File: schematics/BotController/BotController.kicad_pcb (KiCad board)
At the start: 2 copper layers, 29 parts, among them IC1 ATMEGA644A-P, P1 UM2102 - UART2USB, P10 Stepper Upperarm, P11 Stepper Shoulder, P2 Herkulex Servo, P3 Encoder Socket 0, P4 Encoder Socket, P5 Stepper 1 WristTurn, P6 POWER uC, P7 POWER_SERVO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

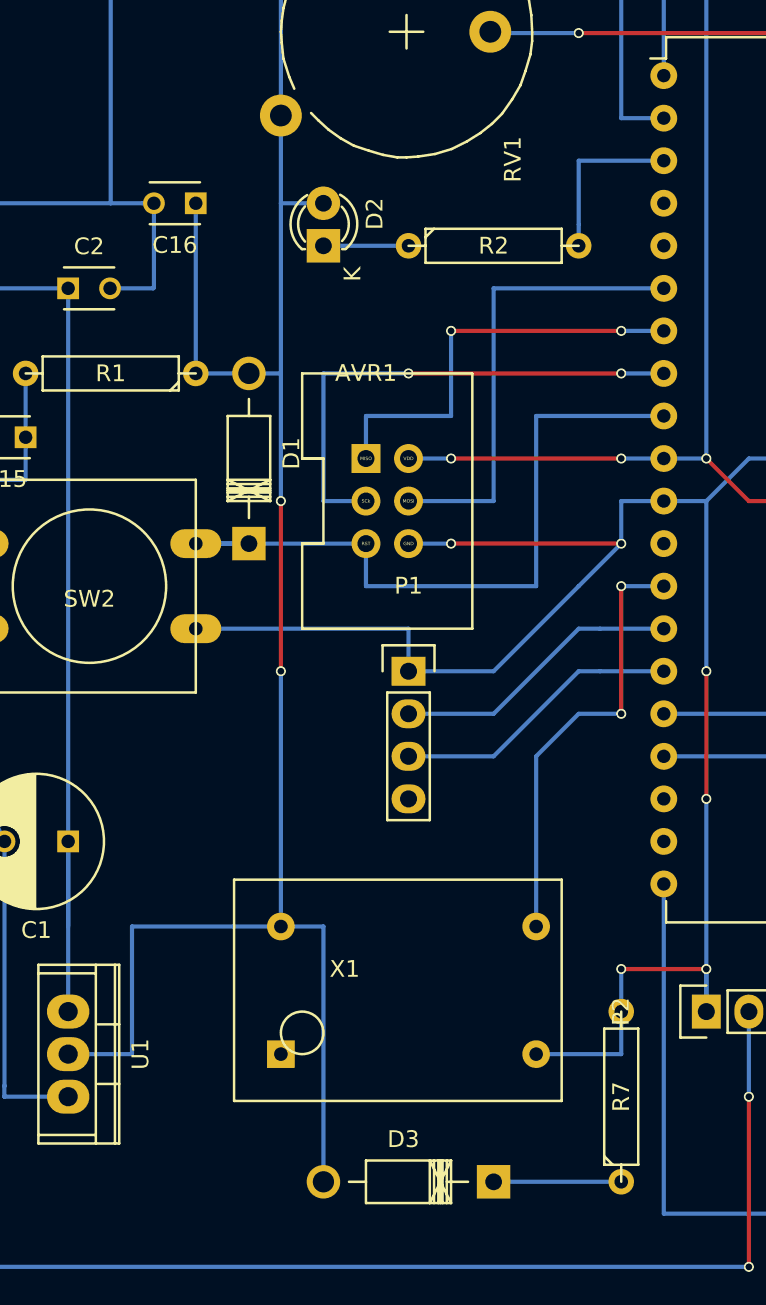
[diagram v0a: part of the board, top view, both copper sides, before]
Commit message: PCB bekommt die letzten 4 PINs als enhancement Stecker Handgelenk vom Rest des entfernbaren Motordecksl bereinigt
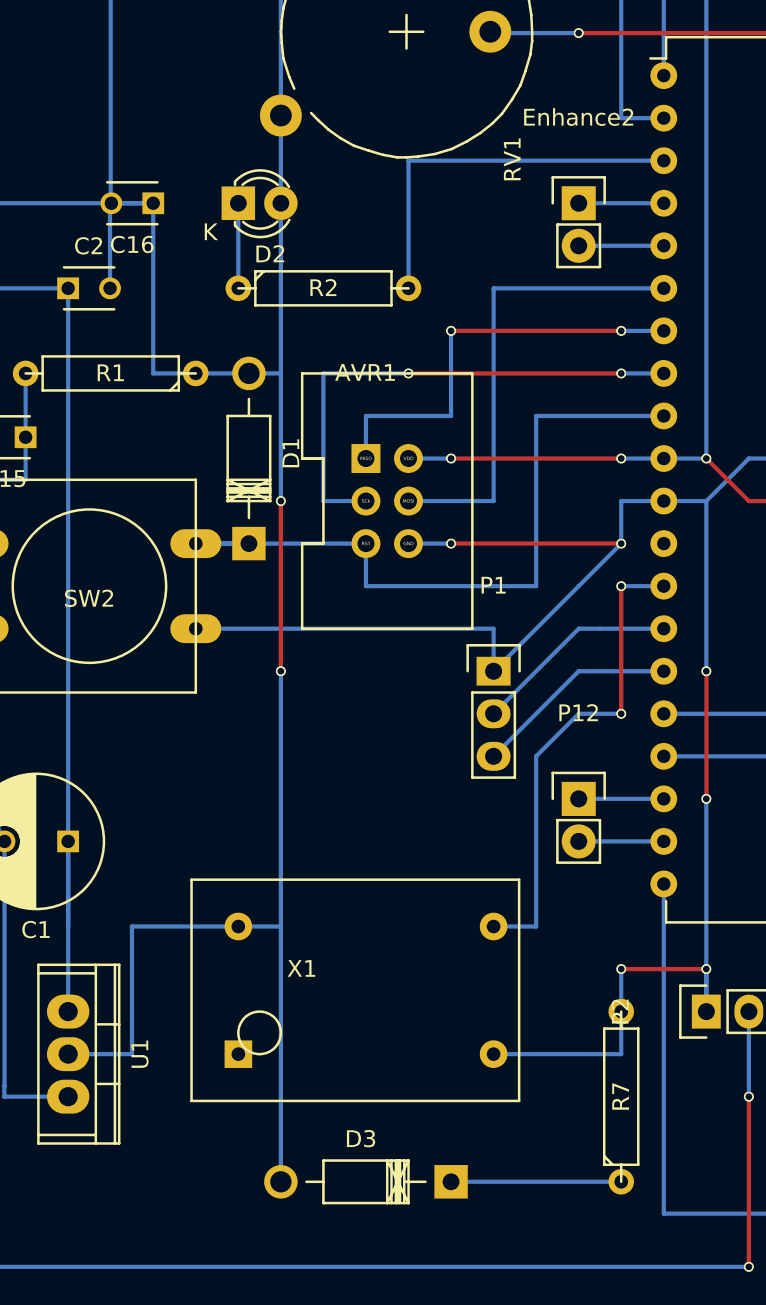
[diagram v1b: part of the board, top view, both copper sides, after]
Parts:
- added Enhance2: CONN_01X02, Pin_Headers:Pin_Header_Straight_1x02, F.Cu at (194.3, 96.5)
- added P12: Enhance1, Pin_Headers:Pin_Header_Straight_1x02, F.Cu at (194.3, 132.1)
- P1: footprint Pin_Headers:Pin_Header_Straight_1x04 -> Pin_Headers:Pin_Header_Straight_1x03
- moved R2 10.5 mm to (179.1, 101.6)
- moved D2 5.68 mm to (174.0, 96.5), turned to 0 degrees
- moved P1 5.08 mm to (189.2, 124.5)
- moved C16 2.54 mm to (168.9, 96.5)
- moved D3 2.54 mm to (186.7, 154.9)
- moved X1 2.54 mm to (177.8, 143.5)
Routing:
- net Net-(IC1-Pad3): track 10.2 -> 22.9 mm
- net Net-(IC1-Pad19): track 0.00 -> 5.08 mm
- net Net-(IC1-Pad18): track 0.00 -> 5.08 mm
- net Net-(Enhance2-Pad2): track 0.00 -> 5.08 mm
- net Net-(Enhance2-Pad1): track 0.00 -> 5.08 mm
- net /TXD0: track 17.3 -> 12.3 mm
- net /RXD0: track 17.3 -> 12.3 mm
- net /TAL: track 26.5 -> 29.0 mm
- net Net-(D3-Pad1): track 7.62 -> 10.2 mm
- net /+5V: track 274.7 -> 272.2 mm
- net GNDPWR: track 395.9 -> 397.0 mm

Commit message: Ellenbogen gedruckt und Schaltung mit PowerSupply gemacht
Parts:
- removed Enhance2: CONN_01X02, Pin_Headers:Pin_Header_Straight_1x02
- added C11: 100uF, Capacitors_ThroughHole:C_Radial_D7.5_L11.2_P2.5, F.Cu at (38.1, 99.1)
- added C12: 100nF, Capacitors_ThroughHole:C_Disc_D3_P2.5, F.Cu at (38.1, 106.7)
- added C13: 1000uF, Capacitors_ThroughHole:C_Radial_D7.5_L11.2_P2.5, F.Cu at (30.5, 116.8)
- added C14: 100nF, Capacitors_ThroughHole:C_Disc_D3_P2.5, F.Cu at (43.2, 119.4)
- added C7: 100uF, Capacitors_ThroughHole:C_Radial_D5_L6_P2.5, F.Cu at (188.0, 92.7)
- added D10: DIODE, Diodes_ThroughHole:Diode_DO-41_SOD81_Horizontal_RM10, F.Cu at (68.6, 119.4)
- added D5: 1N5822, Diodes_ThroughHole:Diode_DO-41_SOD81_Horizontal_RM10, F.Cu at (30.5, 109.2)
- added D9: DIODE, Diodes_ThroughHole:Diode_DO-41_SOD81_Horizontal_RM10, F.Cu at (50.8, 119.4)
- added F1: FUSE, Pin_Headers:Pin_Header_Straight_1x02, F.Cu at (22.9, 96.5)
- added P13: PowerEnableIn, Connectors_Molex:Molex_KK_6410-02, F.Cu at (207.0, 59.7)
- added P17: PowerEnableOut, Connectors_Molex:Molex_KK_6410-02, F.Cu at (61.0, 124.5)
- added P28: Power Stepper, Connect:bornier2, F.Cu at (86.4, 99.1)
- added Q1: Q_NPN_BCE, TO_SOT_Packages_THT:TO-92_Inline_Wide, F.Cu at (48.3, 124.5)
- added Q2: Q_NPN_BCE, TO_SOT_Packages_THT:TO-92_Inline_Wide, F.Cu at (66.0, 124.5)
- added R10: 1K, Discret:R4, F.Cu at (66.0, 129.5)
- added R5: 120, Discret:R4, F.Cu at (81.3, 109.2)
- added R6: 120, Discret:R4, F.Cu at (63.5, 109.2)
- added R8: 1K, Discret:R4, F.Cu at (53.3, 129.5)
- added REL1: Relay_1xON, BotController:RELAIS_HF115F, F.Cu at (55.9, 111.8)
- added REL2: Relay_1xON, BotController:RELAIS_HF115F, F.Cu at (73.7, 111.8)
- added U3: LM7809ACT, Power_Integrations:TO-220, F.Cu at (40.6, 114.3)
- P12: value Enhance1 -> POWER_IN; footprint Pin_Headers:Pin_Header_Straight_1x02 -> Connect:bornier4
- P6: value POWER uC -> Power In uC Servo; footprint Connect:bornier2 -> Connectors_Molex:Molex_KK_6410-03
- P7: value POWER_SERVO -> Power Out uC Servo; footprint Connect:bornier2 -> Connectors_Molex:Molex_KK_6410-03
- moved P12 172.6 mm to (22.9, 111.8), turned to 270 degrees
- moved P7 64.8 mm to (86.4, 114.3), turned to 270 degrees
- moved IC1 39.4 mm to (213.4, 52.1)
- moved P8 39.4 mm to (246.4, 57.1)
- moved R1 39.4 mm to (180.3, 69.8)
- moved R3 39.4 mm to (243.8, 115.6)
- moved R4 39.4 mm to (236.2, 101.6)
- moved R7 39.4 mm to (210.8, 113.0)
- moved AVR1 39.4 mm to (195.6, 74.9)
- moved C1 39.4 mm to (177.8, 97.8)
- moved D1 39.4 mm to (188.6, 80.0)
- moved D2 39.4 mm to (188.0, 59.7)
- moved D3 39.4 mm to (200.7, 118.1)
- moved P1 39.4 mm to (203.2, 87.6)
- moved P10 39.4 mm to (246.4, 77.5)
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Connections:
- C1 pad 1: Net-(C1-Pad1) -> /VDDuC
- C2 pad 1: Net-(C1-Pad1) -> /VDDuC
- IC1 pad 12: Net-(IC1-Pad12) -> (no net)
- IC1 pad 18: Net-(IC1-Pad18) -> (no net)
- IC1 pad 19: Net-(IC1-Pad19) -> (no net)
- P12 pad 1: Net-(IC1-Pad18) -> /24V
- P12 pad 2: Net-(IC1-Pad19) -> /12V
- P2 pad 2: Net-(P2-Pad2) -> /VDDServo
- P6 pad 1: Net-(C1-Pad1) -> GNDPWR
- P6 pad 2: GNDPWR -> /VDDuC
- P7 pad 1: Net-(P2-Pad2) -> /VDD_Servo
- P7 pad 2: GNDPWR -> /VDD_uC
- U1 pad VI: Net-(C1-Pad1) -> /VDDuC
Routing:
- net /VDDServo: track 0.00 -> 132.5 mm, vias 0 -> 2
- net Net-(P2-Pad2): track 114.3 -> 0.00 mm, vias 4 -> 0
- net Net-(C1-Pad1): track 61.0 -> 0.00 mm
- net /VDDuC: track 0.00 -> 61.0 mm
- net GNDPWR: track 397.0 -> 338.7 mm
- net (no net): track 0.00 -> 10.2 mm
- net /RST: track 56.5 -> 65.4 mm
- net /+5V: track 272.2 -> 264.6 mm
- net Net-(IC1-Pad19): track 5.08 -> 0.00 mm
- net Net-(IC1-Pad18): track 5.08 -> 0.00 mm
- net Net-(IC1-Pad4): track 5.08 -> 6.35 mm

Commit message: HostCommunication scheint zu gehen
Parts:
- removed D3, D9: DIODE, Diodes_ThroughHole:Diode_DO-41_SOD81_Horizontal_RM10
- removed R7: 4,7K, Discret:R4
- added C3: 100uF, Capacitors_ThroughHole:C_Radial_D5_L6_P2.5, F.Cu at (88.9, 96.5)
- added C4: 10uF, Capacitors_ThroughHole:C_Radial_D5_L6_P2.5, F.Cu at (71.1, 119.4)
- added C5: 10uF, Capacitors_ThroughHole:C_Radial_D5_L6_P2.5, F.Cu at (64.8, 109.2)
- added D4: D, Diodes_ThroughHole:Diode_DO-35_SOD27_Horizontal_RM10, F.Cu at (185.4, 64.8)
- added P14: ENHANCE, Connectors_Molex:Molex_KK_6410-02, F.Cu at (208.3, 95.2)
- added U2: LM7809ACT, Power_Integrations:TO-220, F.Cu at (86.4, 88.9)
- D1, D10: value DIODE -> Diode; footprint Diodes_ThroughHole:Diode_DO-41_SOD81_Horizontal_RM10 -> Diodes_ThroughHole:Diode_DO-35_SOD27_Horizontal_RM10
- D5: footprint Diodes_ThroughHole:Diode_DO-41_SOD81_Horizontal_RM10 -> Diodes_ThroughHole:Diode_DO-35_SOD27_Horizontal_RM10
- F1: footprint Pin_Headers:Pin_Header_Straight_1x02 -> BotController:FUSE_HOLDER
- P1: footprint Pin_Headers:Pin_Header_Straight_1x03 -> Connectors_Molex:Molex_KK_6410-03
- P10, P11, P2, P3, P4, P5, P8, P9: footprint Pin_Headers:Pin_Header_Straight_1x04 -> Connectors_Molex:Molex_KK_6410-04
- X1: value CRYSTAL_OSSCI -> QUARZ_OSSCILATOR
- moved D1 130.9 mm to (61.0, 109.2), turned to 180 degrees
- moved F1 22.7 mm to (43.2, 86.4), turned to 90 degrees
- moved P28 22.7 mm to (96.5, 119.4), turned to 90 degrees
- moved Q2 20.5 mm to (86.4, 121.9), turned to 90 degrees
- moved C11 19.8 mm to (50.8, 114.3), turned to 90 degrees
- moved P7 18.3 mm to (96.5, 99.1), turned to 90 degrees
- moved P6 18.2 mm to (172.7, 55.9), turned to 180 degrees
- moved D5 16.1 mm to (45.7, 114.3)
- moved D10 12.7 mm to (78.7, 111.8), turned to 180 degrees
- moved C12 11.7 mm to (40.6, 118.1), turned to 180 degrees
- moved C14 10.5 mm to (33.0, 116.8), turned to 270 degrees
- moved R3 10.2 mm to (243.8, 105.4)
- moved R5 10.2 mm to (81.3, 99.1)
- moved P4 8.03 mm to (254.0, 100.3), turned to 180 degrees
- moved P9 8.03 mm to (254.0, 67.3), turned to 180 degrees
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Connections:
- net Net-(IC1-Pad4) renamed /PowerSupplyServo
- net Net-(IC1-Pad5) renamed /PowerSupplyStepper
- C13 pad 1: /VDD_uC -> Net-(C13-Pad1)
- C14 pad 1: /VDD_uC -> Net-(C13-Pad1)
- D1 pad 1: /RST -> Net-(C5-Pad2)
- D1 pad 2: /+5V -> Net-(D1-Pad2)
- D10 pad 1: Net-(D10-Pad1) -> Net-(C4-Pad2)
- D2 pad 1: Net-(D2-Pad1) -> /+5V
- D2 pad 2: /+5V -> Net-(D2-Pad2)
- D5 pad 1: /12V -> Net-(C11-Pad1)
- D5 pad 2: Net-(C11-Pad1) -> /12V
- IC1 pad 18: (no net) -> Net-(IC1-Pad18)
- IC1 pad 19: (no net) -> Net-(IC1-Pad19)
- P10 pad 1: /EN4 -> GNDPWR
- P10 pad 2: /DIR4 -> /CLK4
- P10 pad 3: /CLK4 -> /DIR4
- P10 pad 4: GNDPWR -> /EN4
- P11 pad 1: /En5 -> GNDPWR
- P11 pad 2: /DIR5 -> /CLK5
- P11 pad 3: /CLK5 -> /DIR5
- P11 pad 4: GNDPWR -> /En5
- P17 pad 1: Net-(P17-Pad1) -> /PowerOnStepper
- P17 pad 2: Net-(P17-Pad2) -> /PowerOnServo
- P3 pad 1: /ConflictEncoderVDD -> /ConflictEncoderGND
- P3 pad 2: /SCl -> /SDA
- P3 pad 3: /SDA -> /SCl
- P3 pad 4: /ConflictEncoderGND -> /ConflictEncoderVDD
- P4 pad 1: /+5V -> GNDPWR
- P4 pad 2: /SCl -> /SDA
- P4 pad 3: /SDA -> /SCl
- P4 pad 4: GNDPWR -> /+5V
- P5 pad 1: /EN1 -> GNDPWR
- P5 pad 2: /DIR1 -> /CLK1
- P5 pad 3: /CLK1 -> /DIR1
- P5 pad 4: GNDPWR -> /EN1
- P7 pad 1: /VDD_Servo -> GNDPWR
- P7 pad 3: GNDPWR -> /VDD_Servo
- P8 pad 1: /EN2 -> GNDPWR
- P8 pad 2: /DIR2 -> /CLK2
- P8 pad 3: /CLK2 -> /DIR2
- P8 pad 4: GNDPWR -> /EN2
- P9 pad 1: /EN3 -> GNDPWR
- P9 pad 2: /DIR3 -> /CLK3
- P9 pad 3: /CLK3 -> /DIR3
- P9 pad 4: GNDPWR -> /EN3
- Q1 pad 2: Net-(D9-Pad1) -> Net-(D1-Pad2)
- Q2 pad 2: Net-(D10-Pad1) -> Net-(D10-Pad2)
- R10 pad 2: Net-(P17-Pad1) -> /PowerOnServo
- R2 pad 1: Net-(D2-Pad1) -> Net-(D2-Pad2)
- R5 pad 1: Net-(D10-Pad2) -> Net-(C4-Pad2)
- R6 pad 1: Net-(D9-Pad2) -> Net-(C5-Pad2)
- R8 pad 2: Net-(P17-Pad2) -> /PowerOnStepper
- REL1 pad 1: Net-(D9-Pad1) -> Net-(D1-Pad2)
- REL1 pad 2: Net-(D9-Pad2) -> Net-(C5-Pad2)
- REL1 pad 3: /VDD_uC -> Net-(C13-Pad1)
- REL2 pad 1: Net-(D10-Pad1) -> Net-(D10-Pad2)
- REL2 pad 2: Net-(D10-Pad2) -> Net-(C4-Pad2)
- U3 pad 3: /VDD_uC -> Net-(C13-Pad1)
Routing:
- net Net-(C11-Pad1): track 0.00 -> 109.8 mm
- net Net-(C13-Pad1): track 0.00 -> 63.9 mm
- net GNDPWR: track 338.7 -> 400.3 mm, vias 8 -> 7
- net Net-(P28-Pad1): track 0.00 -> 61.0 mm, vias 0 -> 2
- net /VDD_Servo: track 0.00 -> 48.3 mm
- net /24V: track 0.00 -> 38.1 mm
- net Net-(D10-Pad2): track 0.00 -> 36.8 mm
- net Net-(D1-Pad2): track 0.00 -> 35.6 mm
- net Net-(F1-Pad2): track 0.00 -> 25.4 mm
- net Net-(C4-Pad2): track 0.00 -> 24.7 mm
- net /12V: track 0.00 -> 23.9 mm
- net Net-(C5-Pad2): track 0.00 -> 16.6 mm
- net /+5V: track 264.6 -> 249.3 mm
- net Net-(Q2-Pad1): track 0.00 -> 12.7 mm
- net /VDDuC: track 61.0 -> 72.4 mm
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
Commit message: stepper geht jetzt wieder
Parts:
- P14: value ENHANCE -> Logger
- moved P6 5.68 mm to (175.3, 50.8), turned to 270 degrees
- moved C15 2.54 mm to (175.3, 76.2)
- moved C2 2.54 mm to (172.7, 69.8)
- moved C13 1.27 mm to (26.7, 121.9)
- moved C14 1.27 mm to (31.8, 116.8)
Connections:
- net Net-(IC1-Pad18) renamed /LoggerTX
- IC1 pad 19: Net-(IC1-Pad19) -> (no net)
- P14 pad 2: Net-(IC1-Pad19) -> GNDPWR
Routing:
- net GNDPWR: track 400.3 -> 443.6 mm
- net /ConflictEncoderGND: track 144.8 -> 134.6 mm
- net /RST: track 70.5 -> 61.6 mm
- net Net-(IC1-Pad19): track 5.08 -> 0.00 mm
- net /DIR5: track 83.8 -> 78.7 mm
- net /CLK5: track 106.7 -> 101.6 mm
- net /VDDuC: track 72.4 -> 74.9 mm
- net /VDDServo: track 127.5 -> 125.7 mm, vias 2 -> 0
- net Net-(C13-Pad1): track 63.9 -> 62.6 mm

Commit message: no message
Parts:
- C3: value 100uF -> 220uF
- R3: footprint Discret:R4 -> BotController:R4(8)
- R4: footprint Discret:R5 -> BotController:R4(7)
- moved C2 27.4 mm to (182.9, 95.2), turned to 90 degrees
- moved R3 21.8 mm to (231.1, 87.6), turned to 270 degrees
- moved C15 14.2 mm to (188.0, 82.5), turned to 270 degrees
- moved R4 14.2 mm to (233.7, 87.6), turned to 270 degrees
- moved P2 2.54 mm to (215.9, 113.0)
- moved C16 2.54 mm to (190.5, 97.8)
- moved C7 2.54 mm to (190.5, 92.7)
- moved P10 2.54 mm to (251.5, 77.5)
- moved P11 2.54 mm to (251.5, 87.6)
- moved P3 2.54 mm to (251.5, 110.5)
- moved P4 2.54 mm to (251.5, 100.3)
- moved P5 2.54 mm to (251.5, 47.0)
- moved P8 2.54 mm to (251.5, 57.1)
- moved P9 2.54 mm to (251.5, 67.3)
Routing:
- net /DIR5: track 78.7 -> 27.5 mm, vias 0 -> 2
- net /En5: track 53.3 -> 17.3 mm
- net /SDA: track 76.2 -> 40.6 mm
- net /+5V: track 249.3 -> 228.6 mm, vias 11 -> 9
- net /CLK3: track 38.1 -> 26.6 mm
- net /TAL: track 30.5 -> 40.6 mm
- net /CLK4: track 35.6 -> 25.6 mm
- net /CLK1: track 35.6 -> 25.6 mm
- net /DIR3: track 33.0 -> 23.0 mm
- net /CLK2: track 33.0 -> 24.5 mm
- net /DIR4: track 30.5 -> 22.0 mm
- net /DIR1: track 30.5 -> 22.0 mm
- net /VDDuC: track 74.9 -> 67.3 mm
- net /ConflictEncoderGND: track 134.6 -> 127.0 mm
- net /CLK5: track 101.6 -> 94.0 mm
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
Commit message: kleine Korrekturen beim Ellbogen und unterarm
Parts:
- removed P14: Logger, Connectors_Molex:Molex_KK_6410-02
- P1: value UM2102 - UART2USB -> 2x Serial; footprint Connectors_Molex:Molex_KK_6410-03 -> Sockets_MOLEX_KK-System:Socket_MOLEX-KK-RM2-54mm_Lock_5pin_straight
- moved P1 146.2 mm to (81.3, 154.9)
- moved P13 139.2 mm to (83.8, 121.9)
- moved IC1 136.9 mm to (91.4, 114.3)
- moved P11 136.9 mm to (129.5, 149.9)
- moved P3 136.9 mm to (129.5, 172.7)
- moved P4 136.9 mm to (129.5, 162.6)
- moved P5 136.9 mm to (129.5, 109.2)
- moved P8 136.9 mm to (129.5, 119.4)
- moved U1 136.9 mm to (55.9, 172.7)
- moved AVR1 136.9 mm to (73.7, 137.2)
- moved D2 136.9 mm to (68.6, 121.9)
- moved D4 136.9 mm to (63.5, 127.0)
- moved P10 136.9 mm to (129.5, 139.7)
- moved P2 136.9 mm to (94.0, 175.3)
- moved P6 136.9 mm to (53.3, 113.0)
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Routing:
- net GNDPWR: track 436.2 -> 577.6 mm, vias 8 -> 10
- net /24V: track 38.1 -> 12.7 mm
- net /VDDServo: track 125.7 -> 110.5 mm
- net Net-(C11-Pad1): track 109.8 -> 96.5 mm, vias 0 -> 2
- net /12V: track 23.9 -> 14.0 mm
- net Net-(C13-Pad1): track 62.6 -> 71.1 mm
- net /VDD_uC: track 7.62 -> 15.2 mm
- net Net-(F1-Pad2): track 25.4 -> 33.0 mm
- net /RST: track 64.1 -> 56.9 mm
- net /RXD0: track 5.08 -> 12.3 mm
- net /TXD0: track 5.08 -> 12.3 mm
- net /LoggerTX: track 5.08 -> 11.2 mm
- net /+5V: track 228.6 -> 233.7 mm
- net /PowerOnStepper: track 0.00 -> 5.08 mm
- net /TAL: track 40.6 -> 35.6 mm
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
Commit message: PCB angefangen
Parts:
- added C6: 100nF, Capacitors_ThroughHole:C_Disc_D3_P2.5, F.Cu at (119.4, 57.1)
- C11: value 100uF -> 2200uF
- P6: footprint Connectors_Molex:Molex_KK_6410-03 -> Connect:bornier3
- R3, R4: value 1.5K -> 4.7K
- RV1: footprint Potentiometers:Potentiometer_Trimmer-Piher_PT15-V12-5_horizontal -> BotController:Potentiometer_Trimmer-ALPS-horizontal
- moved C16 29.0 mm to (88.9, 137.2), turned to 270 degrees
- moved R2 8.03 mm to (73.7, 119.4)
- moved D2 5.68 mm to (63.5, 119.4), turned to 0 degrees
- moved RV1 5.08 mm to (68.6, 109.2)
- moved P2 2.54 mm to (94.0, 172.7)
- moved U1 2.54 mm to (55.9, 170.2)
- moved P6 1.27 mm to (53.3, 114.3)
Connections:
- D2 pad 1: /+5V -> GNDPWR
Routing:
- net Net-(IC1-Pad40): track 30.7 -> 45.7 mm
- net /+5V: track 233.7 -> 241.3 mm
- net Net-(IC1-Pad3): track 22.9 -> 17.8 mm
- net GNDPWR: track 577.6 -> 572.6 mm
- net Net-(D2-Pad2): track 5.08 -> 2.54 mm
- net /TXD1: track 30.5 -> 27.9 mm
- net /RXD1: track 30.5 -> 27.9 mm
- net /VDDuC: track 66.0 -> 64.8 mm
- net /VDDServo: track 110.5 -> 111.8 mm

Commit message: no message
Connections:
- P1 pad 4: (no net) -> GNDPWR
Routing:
- net GNDPWR: track 572.6 -> 585.5 mm
- net /DIR5: track 27.5 -> 30.5 mm
- net /RST: track 56.9 -> 58.4 mm
